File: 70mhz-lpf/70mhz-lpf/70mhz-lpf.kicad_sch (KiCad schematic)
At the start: 16 parts, among them J701 Coax Solder Point, J702 Coax Solder Point

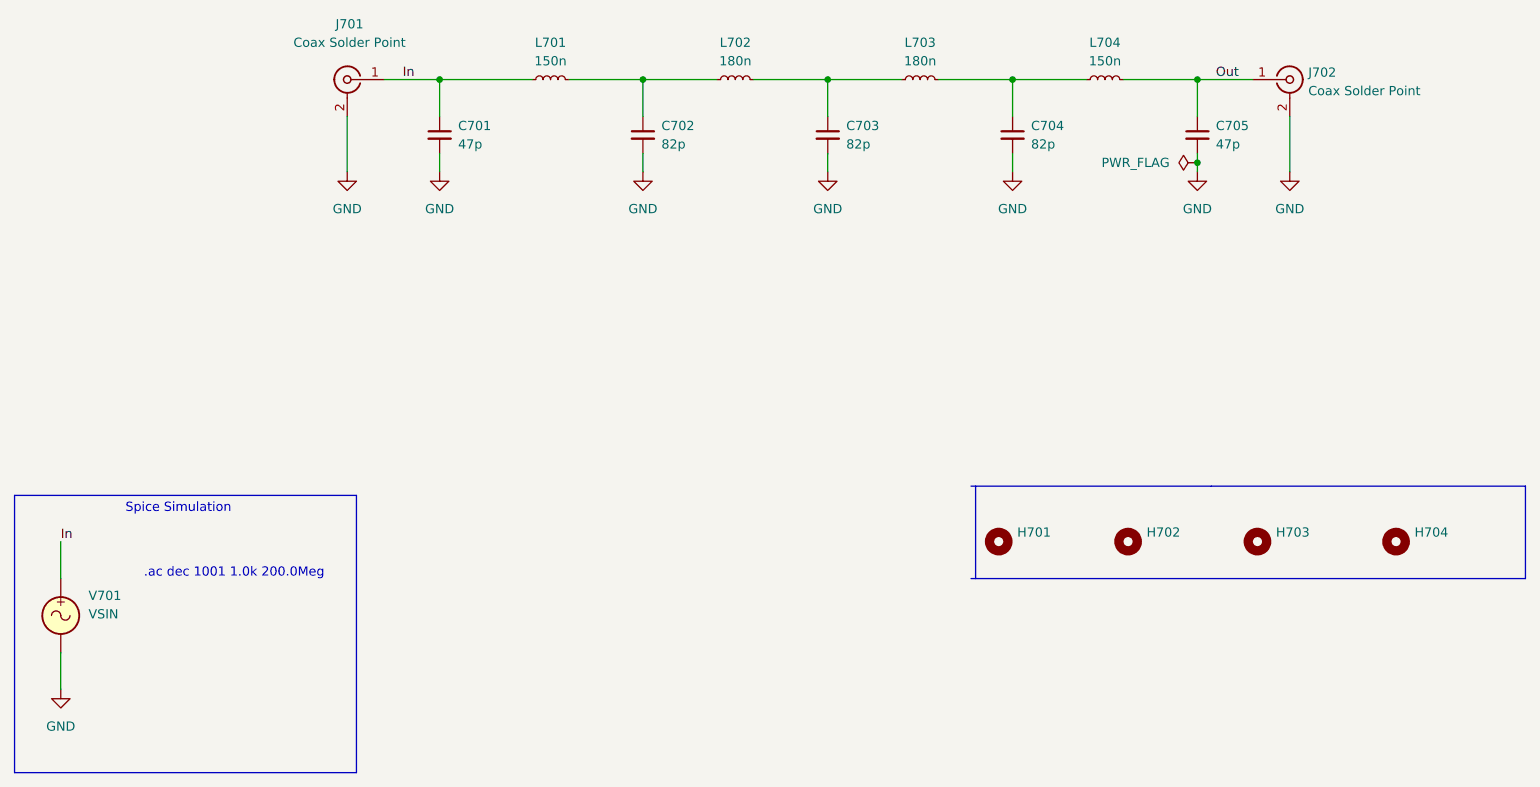
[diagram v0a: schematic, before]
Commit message: 70Mhz spice models
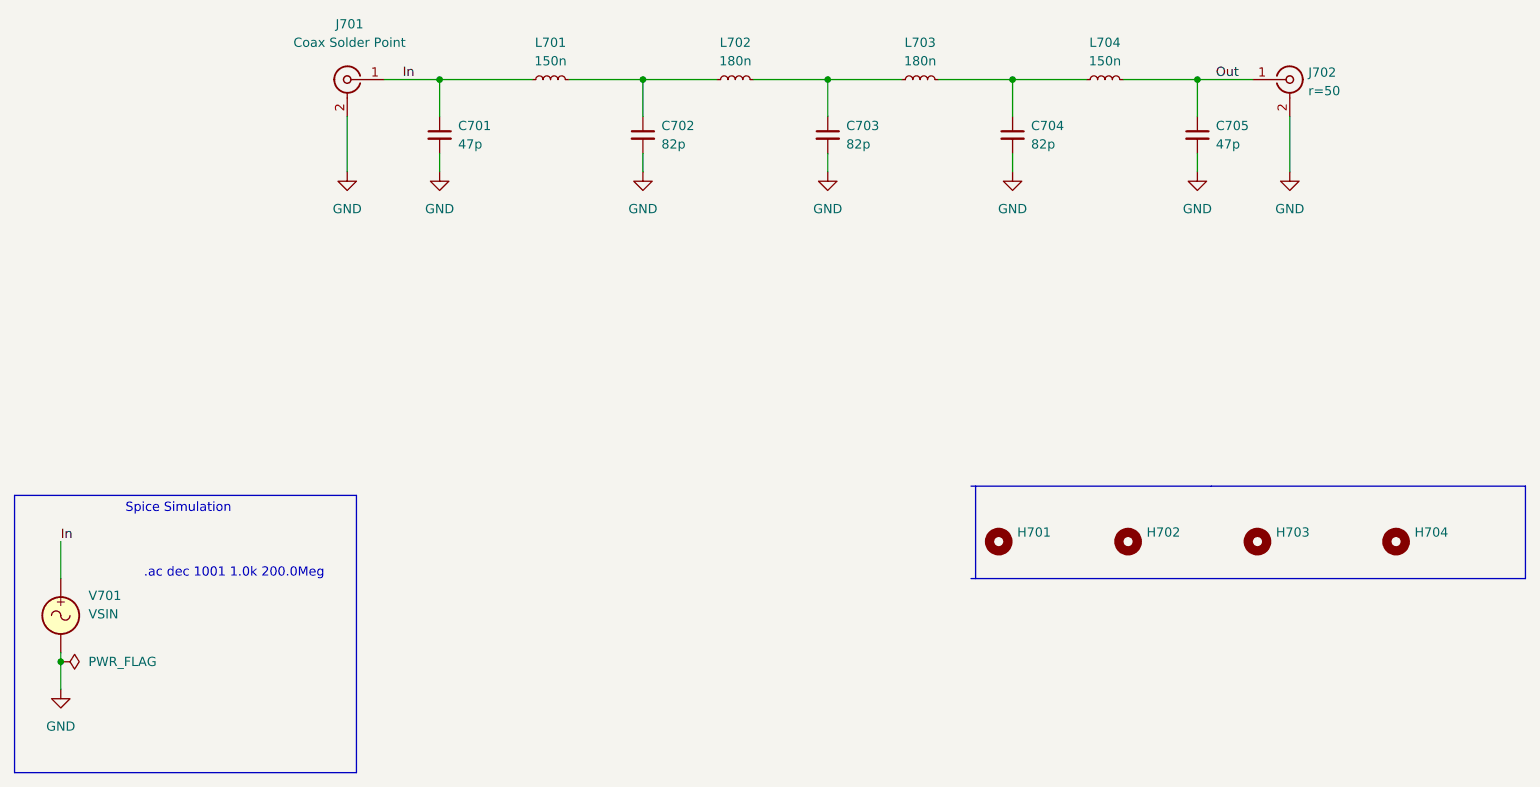
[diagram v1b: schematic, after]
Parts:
- J702: value Coax Solder Point -> ${SIM.PARAMS}
